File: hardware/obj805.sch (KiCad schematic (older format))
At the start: 1 part, among them J0 Conn_with_rapi

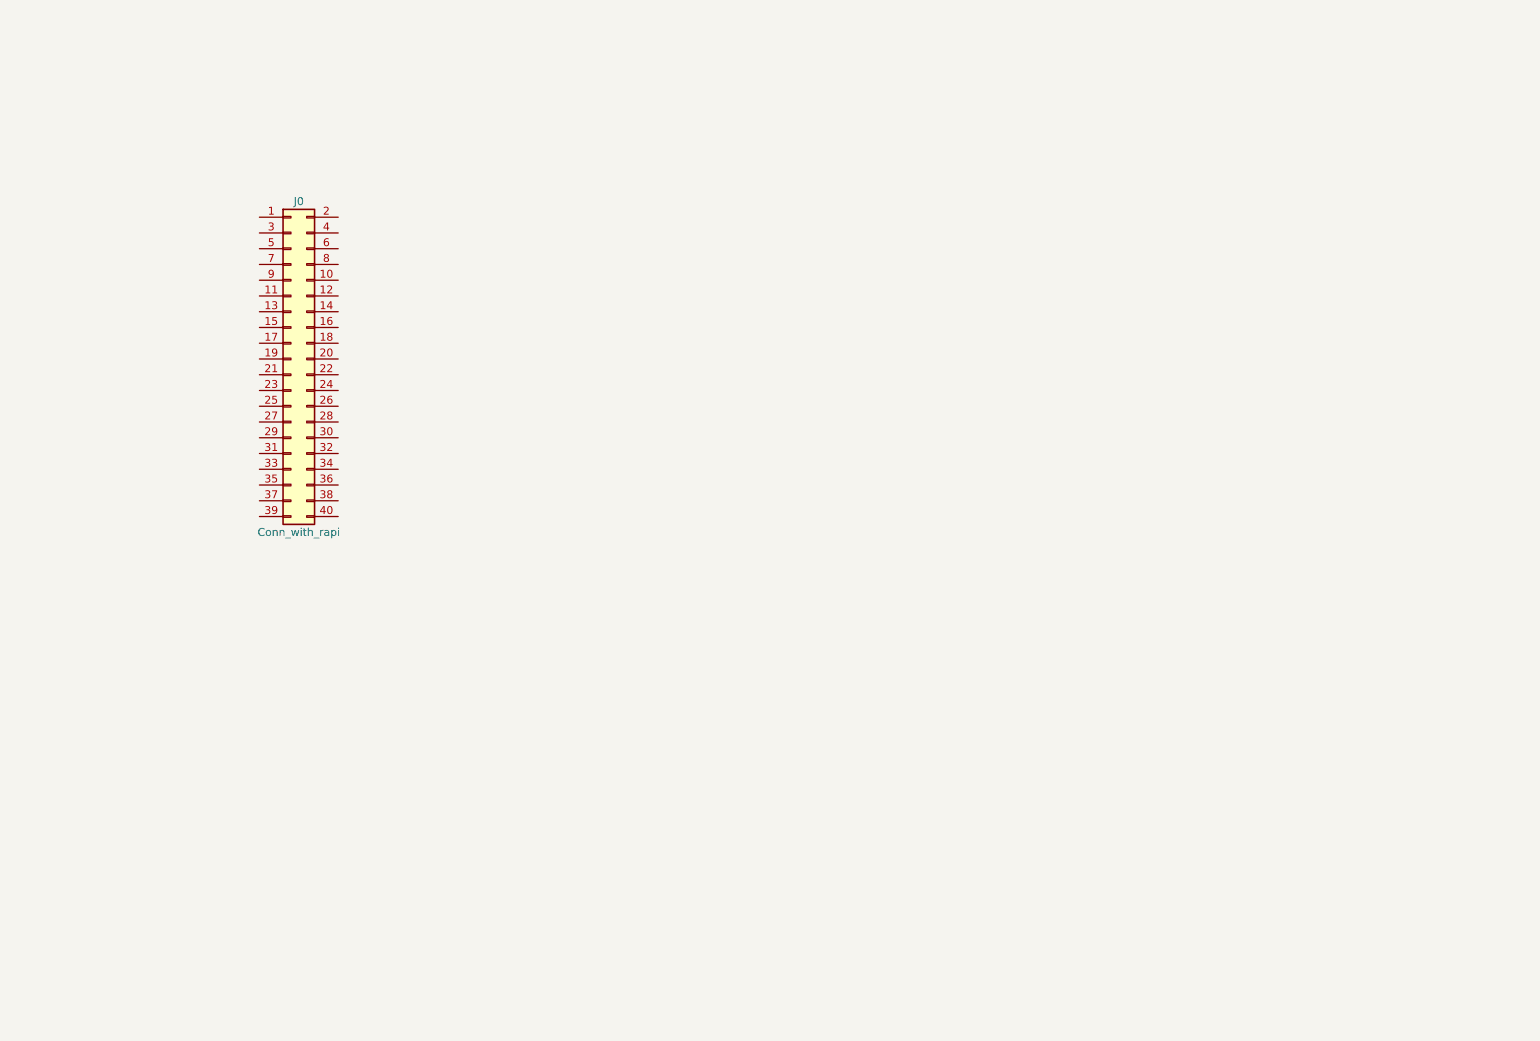
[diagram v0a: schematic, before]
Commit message: add l293d, and connect the circut(undone)
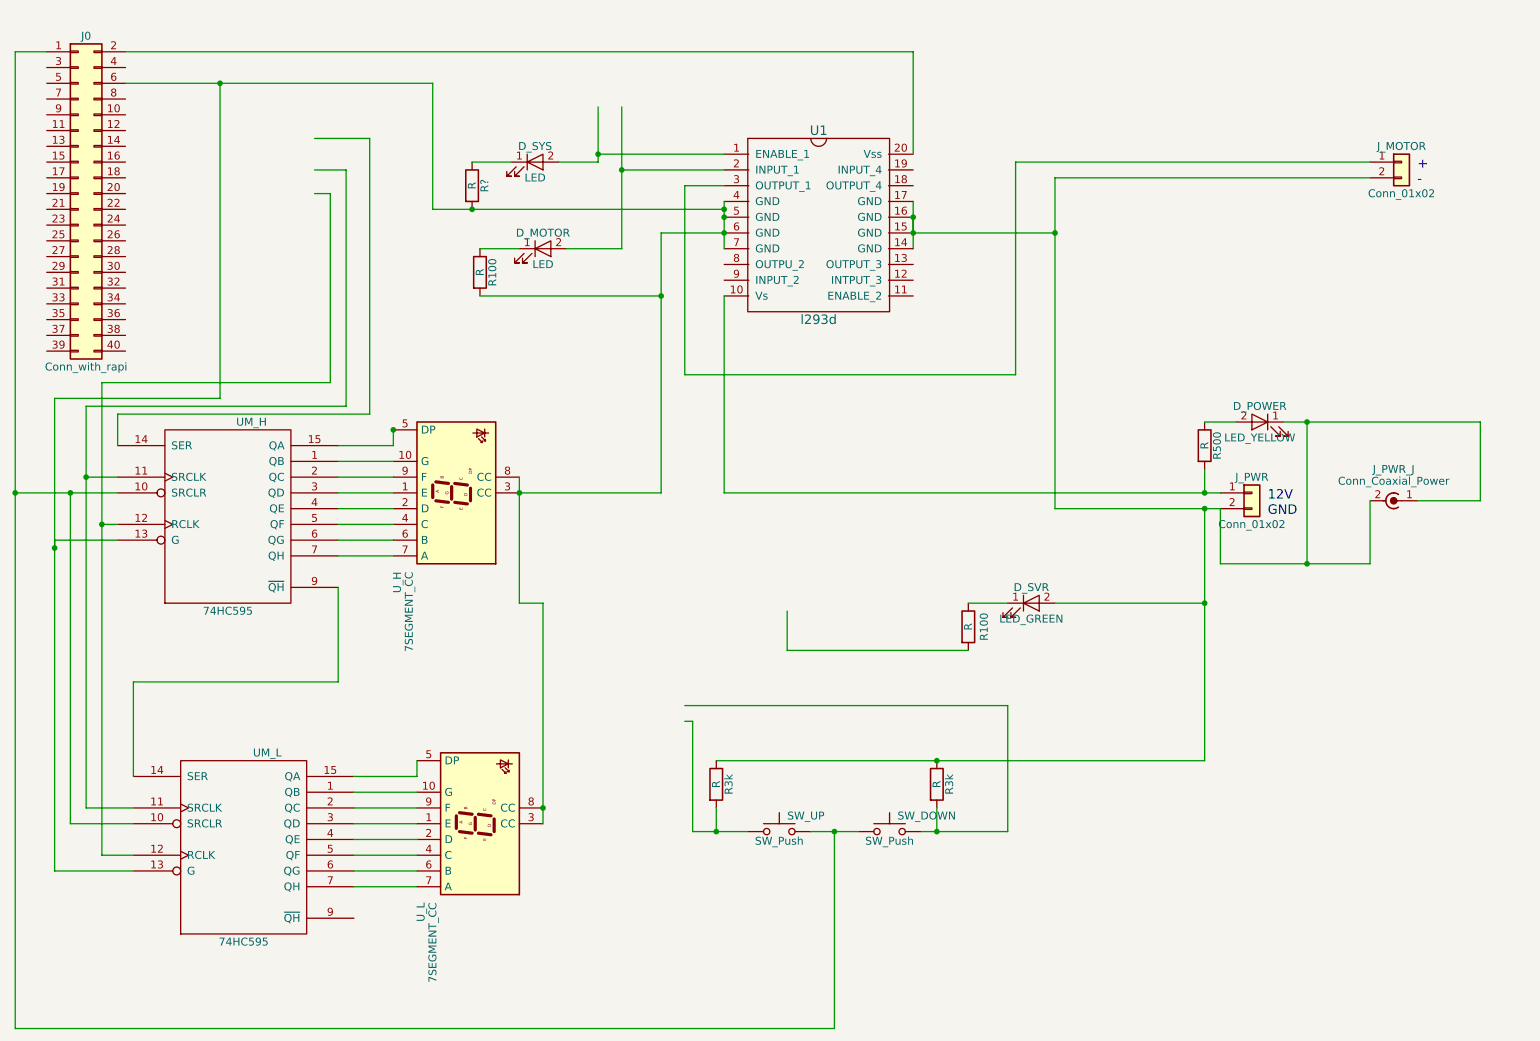
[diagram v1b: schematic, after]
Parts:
- added D_MOTOR, D_SYS: LED, symbol LED
- added D_POWER: LED_YELLOW, symbol LED
- added D_SVR: LED_GREEN, symbol LED
- added J_MOTOR, J_PWR: Conn_01x02, symbol Conn_01x02
- added J_PWR_J: Conn_Coaxial_Power, symbol Conn_Coaxial_Power
- added R100 (x2), R3k (x2), R500, R?: R, symbol R
- added SW_DOWN, SW_UP: SW_Push, symbol SW_Push
- added U1: l293d, symbol l293d
- added UM_H, UM_L: 74HC595, symbol 74HC595
- added U_H, U_L: 7SEGMENT_CC, symbol 7SEGMENT_CC
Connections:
- wire segments 0 -> 108
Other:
- note added: "+\n-"
- note added: "12V\nGND"
- moved on the sheet: J0

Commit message: update
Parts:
- removed J_PWR_J: Conn_Coaxial_Power, symbol Conn_Coaxial_Power
- added J_PWR_J2: Jack-DC, Connectors:JACK_ALIM, symbol Jack-DC
- added R10, R11, R12, R13, R14, R15, R16, R17, R2, R3, R4, R5, R6, R7, R8, R9: R, Resistors_SMD:R_0805, symbol R
- D_MOTOR1: renamed from D_MOTOR; footprint (none) -> LEDs:LED_1206
- D_POWER1: renamed from D_POWER; footprint (none) -> LEDs:LED_1206
- D_SVR1: renamed from D_SVR; footprint (none) -> LEDs:LED_1206
- D_SYS1: renamed from D_SYS; footprint (none) -> LEDs:LED_1206
- J0: footprint (none) -> Pin_Headers:Pin_Header_Straight_2x20_Pitch2.54mm
- J_MOTOR1: renamed from J_MOTOR; footprint (none) -> Pin_Headers:Pin_Header_Straight_1x02_Pitch2.54mm
- J_PWR1: renamed from J_PWR; footprint (none) -> Pin_Headers:Pin_Header_Straight_1x02_Pitch2.54mm
- R1: renamed from R?; footprint (none) -> Resistors_SMD:R_0805
- R100_1, R100_2: renamed from R100; footprint (none) -> Resistors_SMD:R_0805
- R3k1, R3k2: renamed from R3k; footprint (none) -> Resistors_SMD:R_0805
- R500: footprint (none) -> Resistors_SMD:R_0805
- SW_DOWN1: renamed from SW_DOWN; footprint (none) -> Buttons_Switches_THT:SW_PUSH_6mm
- SW_UP1: renamed from SW_UP; footprint (none) -> Buttons_Switches_THT:SW_PUSH_6mm
- U1: footprint (none) -> l293d:SOIC-20
- UM_H1: renamed from UM_H; footprint (none) -> SMD_Packages:SO-16-N
- UM_L1: renamed from UM_L; footprint (none) -> SMD_Packages:SO-16-N
- U_H1: renamed from U_H; footprint (none) -> l293d:7SegmentLED_3611
- U_L1: renamed from U_L; footprint (none) -> l293d:7SegmentLED_3611
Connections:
- wire segments 108 -> 135

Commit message: update
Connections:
- net at J0.6 (Pin_6), R1.2, R100_2.2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: now also D_POWER1.1 (K), D_SVR1.1 (K), J_MOTOR1.2 (Pin_2), J_PWR1.2 (Pin_2), J_PWR_J2.2, J_PWR_J2.3, R3k1.1, R3k2.1, U1.14 (GND), U1.15 (GND), U1.16 (GND), U1.17 (GND)
- net at R100_1.1: now also D_SVR1.2 (A); no longer D_SVR1.1 (K)
- net at UM_L1.1 (QB): now also R14.2; no longer R11.2
- net at UM_L1.2 (QC): now also R13.2; no longer R12.2
- net at UM_L1.3 (QD): now also R11.2; no longer R13.2
- net at UM_L1.4 (QE): now also R12.2; no longer R14.2
- net at UM_L1.5 (QF): now also R17.2; no longer R15.2
- net at UM_L1.7 (QH): now also R15.2; no longer R17.2
- net at UM_H1.1 (QB): now also R6.2; no longer R3.2
- net at UM_H1.2 (QC): now also R5.2; no longer R4.2
- net at UM_H1.3 (QD): now also R3.2; no longer R5.2
- net at UM_H1.4 (QE): now also R4.2; no longer R6.2
- net at UM_H1.5 (QF): now also R9.2; no longer R7.2
- net at UM_H1.7 (QH): now also R7.2; no longer R9.2
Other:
- moved on the sheet: D_SVR1, R10, R11, R12, R13, R14, R15, R16, R17, R2, R3, R4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

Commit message: update
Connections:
- net at J0.16 (Pin_16): now also UM_H1.11 (SRCLK), UM_L1.11 (SRCLK); no longer UM_H1.14 (SER)
- net at UM_H1.12 (RCLK), UM_L1.12 (RCLK): now also J0.18 (Pin_18); no longer J0.22 (Pin_22)
- new net: J0.22 (Pin_22), UM_H1.14 (SER)
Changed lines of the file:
@@
 	1000 5800 1400 5800
 Wire Wire Line
-	1100 5700 1400 5700
-Wire Wire Line
-	1100 3150 1100 5700
+	1100 3300 1100 5700
 Wire Wire Line
 	1100 3600 1300 3600
@@
 	1300 3900 1200 3900
 Wire Wire Line
-	1200 3000 1200 6000
+	1200 3250 1200 6000
 Wire Wire Line
 	1200 6000 1400 6000
@@
 Connection ~ 900  4050
 Wire Wire Line
-	1300 3400 1300 3200
-Wire Wire Line
-	1300 3200 2900 3200
-Wire Wire Line
-	2900 3200 2900 1450
-Wire Wire Line
-	2900 1450 1650 1450
-Wire Wire Line
-	1100 3150 2750 3150
-Wire Wire Line
-	2750 3150 2750 1650
-Wire Wire Line
-	2750 1650 1750 1650
-Connection ~ 1100 3600
-Wire Wire Line
-	1200 3000 2650 3000
-Wire Wire Line
-	2650 3000 2650 1800
-Wire Wire Line
-	2650 1800 1600 1800
-Connection ~ 1200 3900
-Wire Wire Line
 	7250 4400 8200 4400
 Wire Wire Line
@@
 	700  1200 850  1200
 Wire Wire Line
-	1650 1450 1650 1600
-Wire Wire Line
-	1650 1600 1350 1600
-Wire Wire Line
-	1750 1650 1750 1700
-Wire Wire Line
-	1750 1700 1350 1700
-Wire Wire Line
-	1600 1800 1600 1900
-Wire Wire Line
-	1600 1900 1350 1900
-Wire Wire Line
 	5550 4450 4200 4450
 Wire Wire Line
@@
 Wire Wire Line
 	5150 1950 6350 1950
+Wire Wire Line
+	1100 5700 1400 5700
+Wire Wire Line
+	1350 1600 1500 1600
+Wire Wire Line
+	1500 1600 1500 3300
+Wire Wire Line
+	1500 3300 1100 3300
+Connection ~ 1100 3600
+Wire Wire Line
+	1350 1700 1650 1700
+Wire Wire Line
+	1650 1700 1650 3250
+Wire Wire Line
+	1650 3250 1200 3250
+Connection ~ 1200 3900
+Wire Wire Line
+	1400 1900 1350 1900
+Wire Wire Line
+	1400 1900 1400 3050
+Wire Wire Line
+	1400 3050 1300 3050
+Wire Wire Line
+	1300 3050 1300 3400
 $EndSCHEMATC

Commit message: update;
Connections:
- net at UM_L1.1 (QB): now also R15.2; no longer R14.2
- net at UM_L1.2 (QC): now also R16.2; no longer R13.2
- net at UM_L1.3 (QD): now also R17.2; no longer R11.2
- net at UM_L1.5 (QF): now also R11.2; no longer R17.2
- net at UM_L1.6 (QG): now also R13.2; no longer R16.2
- net at UM_L1.7 (QH): now also R14.2; no longer R15.2
- net at UM_H1.1 (QB): now also R7.2; no longer R6.2
- net at UM_H1.2 (QC): now also R8.2; no longer R5.2
- net at UM_H1.3 (QD): now also R9.2; no longer R3.2
- net at UM_H1.5 (QF): now also R3.2; no longer R9.2
- net at UM_H1.6 (QG): now also R5.2; no longer R8.2
- net at UM_H1.7 (QH): now also R6.2; no longer R7.2
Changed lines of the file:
@@
 	3700 3300 3700 3400
-Wire Wire Line
-	2700 3400 3400 3400
-Wire Wire Line
-	2700 3500 3000 3500
-Wire Wire Line
-	3000 3500 3000 3800
-Wire Wire Line
-	3000 3800 3400 3800
-Wire Wire Line
-	2700 3600 3050 3600
-Wire Wire Line
-	3050 3600 3050 3700
-Wire Wire Line
-	3050 3700 3400 3700
-Wire Wire Line
-	2700 3700 2900 3700
-Wire Wire Line
-	2900 3700 2900 3550
-Wire Wire Line
-	2900 3550 3250 3550
-Wire Wire Line
-	3250 3550 3250 3500
-Wire Wire Line
-	3250 3500 3400 3500
-Wire Wire Line
-	2700 3800 2950 3800
-Wire Wire Line
-	2950 3800 2950 3750
-Wire Wire Line
-	2950 3750 3300 3750
-Wire Wire Line
-	3300 3750 3300 3600
-Wire Wire Line
-	3300 3600 3400 3600
-Wire Wire Line
-	2700 3900 3150 3900
-Wire Wire Line
-	3150 3900 3150 4100
-Wire Wire Line
-	3150 4100 3400 4100
-Wire Wire Line
-	2700 4000 3400 4000
-Wire Wire Line
-	2700 4100 3000 4100
-Wire Wire Line
-	3000 4100 3000 3950
-Wire Wire Line
-	3000 3950 3250 3950
-Wire Wire Line
-	3250 3950 3250 3900
-Wire Wire Line
-	3250 3900 3400 3900
 Wire Wire Line
 	4500 3600 4500 4700
 Wire Wire Line
 	3800 5400 3800 5500
-Wire Wire Line
-	2800 5500 3500 5500
-Wire Wire Line
-	2800 5600 3000 5600
-Wire Wire Line
-	3000 5600 3000 5900
-Wire Wire Line
-	3000 5900 3500 5900
-Wire Wire Line
-	2800 5700 3250 5700
-Wire Wire Line
-	3250 5700 3250 5800
-Wire Wire Line
-	3250 5800 3500 5800
-Wire Wire Line
-	2800 5800 3050 5800
-Wire Wire Line
-	3050 5800 3050 5600
-Wire Wire Line
-	3050 5600 3500 5600
-Wire Wire Line
-	2800 5900 2950 5900
-Wire Wire Line
-	2950 5900 2950 5850
-Wire Wire Line
-	2950 5850 3350 5850
-Wire Wire Line
-	3350 5850 3350 5700
-Wire Wire Line
-	3350 5700 3500 5700
-Wire Wire Line
-	2800 6000 3400 6000
-Wire Wire Line
-	3400 6000 3400 6200
-Wire Wire Line
-	3400 6200 3500 6200
-Wire Wire Line
-	2800 6200 2900 6200
-Wire Wire Line
-	2900 6200 2900 6050
-Wire Wire Line
-	2900 6050 3500 6050
-Wire Wire Line
-	3500 6050 3500 6000
-Wire Wire Line
-	2800 6100 3500 6100
 Wire Wire Line
 	4600 4700 4600 5800
@@
 Wire Wire Line
 	1300 3050 1300 3400
+Wire Wire Line
+	2700 3400 3400 3400
+Wire Wire Line
+	2700 3500 3100 3500
+Wire Wire Line
+	3100 3500 3100 3900
+Wire Wire Line
+	3100 3900 3400 3900
+Wire Wire Line
+	2700 3600 3050 3600
+Wire Wire Line
+	3050 3600 3050 4000
+Wire Wire Line
+	3050 4000 3400 4000
+Wire Wire Line
+	2700 3700 3000 3700
+Wire Wire Line
+	3000 3700 3000 4100
+Wire Wire Line
+	3000 4100 3400 4100
+Wire Wire Line
+	2700 3800 3150 3800
+Wire Wire Line
+	3150 3800 3150 3600
+Wire Wire Line
+	3150 3600 3400 3600
+Wire Wire Line
+	2700 3900 2900 3900
+Wire Wire Line
+	2900 3900 2900 3550
+Wire Wire Line
+	2900 3550 3350 3550
+Wire Wire Line
+	3350 3550 3350 3500
+Wire Wire Line
+	3350 3500 3400 3500
+Wire Wire Line
+	2700 4000 2950 4000
+Wire Wire Line
+	2950 4000 2950 3950
+Wire Wire Line
+	2950 3950 3250 3950
+Wire Wire Line
+	3250 3950 3250 3700
+Wire Wire Line
+	3250 3700 3400 3700
+Wire Wire Line
+	2700 4100 2900 4100
+Wire Wire Line
+	2900 4100 2900 4150
+Wire Wire Line
+	2900 4150 3350 4150
+Wire Wire Line
+	3350 4150 3350 3800
+Wire Wire Line
+	3350 3800 3400 3800
+Wire Wire Line
+	2800 5500 3500 5500
+Wire Wire Line
+	2800 5600 3200 5600
+Wire Wire Line
+	3200 5600 3200 6000
+Wire Wire Line
+	3200 6000 3500 6000
+Wire Wire Line
+	2800 5700 3150 5700
+Wire Wire Line
+	3150 5700 3150 6100
+Wire Wire Line
+	3150 6100 3500 6100
+Wire Wire Line
+	2800 5800 3100 5800
+Wire Wire Line
+	3100 5800 3100 6200
+Wire Wire Line
+	3100 6200 3500 6200
+Wire Wire Line
+	2800 5900 3250 5900
+Wire Wire Line
+	3250 5900 3250 5700
+Wire Wire Line
+	3250 5700 3500 5700
+Wire Wire Line
+	2800 6000 3000 6000
+Wire Wire Line
+	3000 6000 3000 5650
+Wire Wire Line
+	3000 5650 3450 5650
+Wire Wire Line
+	3450 5650 3450 5600
+Wire Wire Line
+	3450 5600 3500 5600
+Wire Wire Line
+	2800 6100 3050 6100
+Wire Wire Line
+	3050 6100 3050 6050
+Wire Wire Line
+	3050 6050 3350 6050
+Wire Wire Line
+	3350 6050 3350 5800
+Wire Wire Line
+	3350 5800 3500 5800
+Wire Wire Line
+	2800 6200 3000 6200
+Wire Wire Line
+	3000 6200 3000 6250
+Wire Wire Line
+	3000 6250 3450 6250
+Wire Wire Line
+	3450 6250 3450 5900
+Wire Wire Line
+	3450 5900 3500 5900
 $EndSCHEMATC

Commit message: update
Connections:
- net GND: now also D_POWER1.1 (K), D_SVR1.1 (K), J0.6 (Pin_6), J_MOTOR1.2 (Pin_2), J_PWR1.2 (Pin_2), J_PWR_J2.2, J_PWR_J2.3, R1.2, R100_2.2, R3k1.1, R3k2.1, U1.14 (GND), U1.15 (GND), U1.16 (GND), U1.17 (GND), U1.4 (GND), U1.5 (GND), U1.6 (GND), U1.7 (GND), UM_H1.13 (G), UM_L1.13 (G), U_H1.3 (CC), U_H1.8 (CC), U_L1.3 (CC), U_L1.8 (CC)
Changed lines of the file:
@@
 Wire Wire Line
 	3450 5900 3500 5900
+Wire Wire Line
+	1800 6500 8050 6500
+Wire Wire Line
+	8050 6500 8050 3800
+Connection ~ 8050 3800
 $EndSCHEMATC

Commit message: update
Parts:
- removed D_MOTOR1, D_SYS1: LED, LEDs:LED_1206, symbol LED
- removed D_POWER1: LED_YELLOW, LEDs:LED_1206, symbol LED
- removed D_SVR1: LED_GREEN, LEDs:LED_1206, symbol LED
- removed J_MOTOR1, J_PWR1: Conn_01x02, Pin_Headers:Pin_Header_Straight_1x02_Pitch2.54mm, symbol Conn_01x02
- removed J_PWR_J2: Jack-DC, Connectors:JACK_ALIM, symbol Jack-DC
- removed R1, R10, R100_1, R100_2, R11, R12, R13, R14, R15, R16, R17, R2, R3, R3k1, R3k2, R4, R5, R500, R6, R7, R8, R9: R, Resistors_SMD:R_0805, symbol R
- removed SW_DOWN1, SW_UP1: SW_Push, Buttons_Switches_THT:SW_PUSH_6mm, symbol SW_Push
- removed U1: l293d, l293d:SOIC-20, symbol l293d
- removed UM_H1, UM_L1: 74HC595, SMD_Packages:SO-16-N, symbol 74HC595
- removed U_H1, U_L1: 7SEGMENT_CC, l293d:7SegmentLED_3611, symbol 7SEGMENT_CC
- added F0: Conn_01x02, Pin_Headers:Pin_Header_Straight_1x02_Pitch2.54mm, symbol Conn_01x02
- added P0: Jack-DC, Connectors:JACK_ALIM, symbol Jack-DC
- added U1: L293D, l293d:L293D, symbol L293D
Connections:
- net GND is gone; now on an unnamed net: J0.6 (Pin_6)
- net at J0.14 (Pin_14): now also J0.20 (Pin_20), J0.25 (Pin_25), J0.30 (Pin_30), J0.34 (Pin_34), J0.39 (Pin_39), J0.9 (Pin_9), F0.2 (Pin_2), P0.2, P0.3, U1.12 (GND), U1.13 (GND), U1.4 (GND), U1.5 (GND)
- net at J0.2 (Pin_2): now also J0.4 (Pin_4), U1.16 (Vss)
- net at J0.35 (Pin_35): now also U1.2 (INPUT1)
- net at J0.7 (Pin_7): now also U1.1 (ENABLE1,2)
- new net: P0.1, U1.8 (Vs)
- new net: F0.1 (Pin_1), U1.3 (OUTPUT1)
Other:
- note removed: "+\n-"
- note removed: "12V\nGND"
